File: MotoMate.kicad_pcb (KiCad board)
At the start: 2 copper layers, 92.3 x 50.2 mm, 62 parts, among them CN1 Cin1, CN2 Cin2, J1 Prog, J2 uUSB, J3 microSD, J4 GPS, J5 AUX_UART, J6 AUX_I2C, J7 Battery, J8 ILI9341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

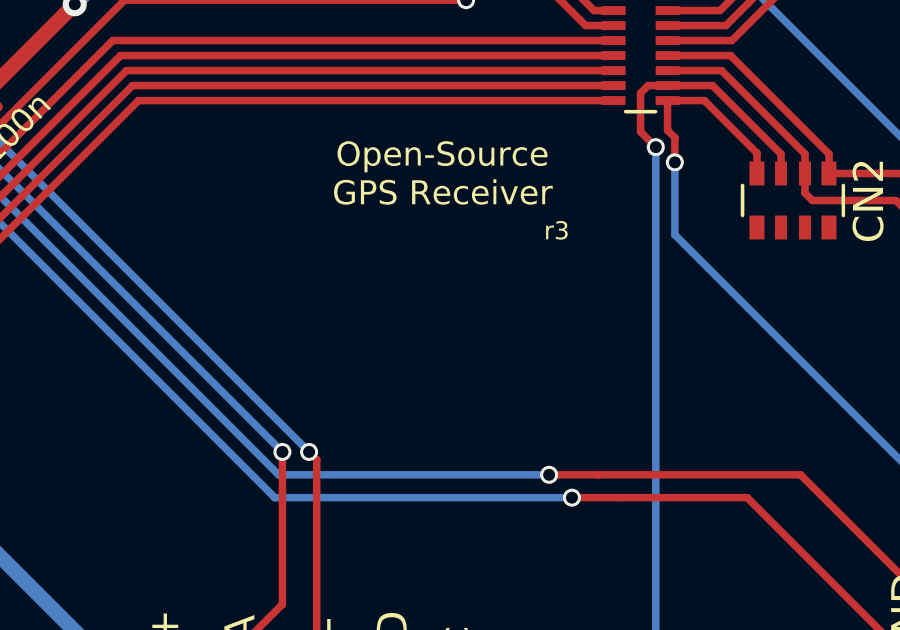
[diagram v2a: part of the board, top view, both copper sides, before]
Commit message: Re-add the OSHW logo
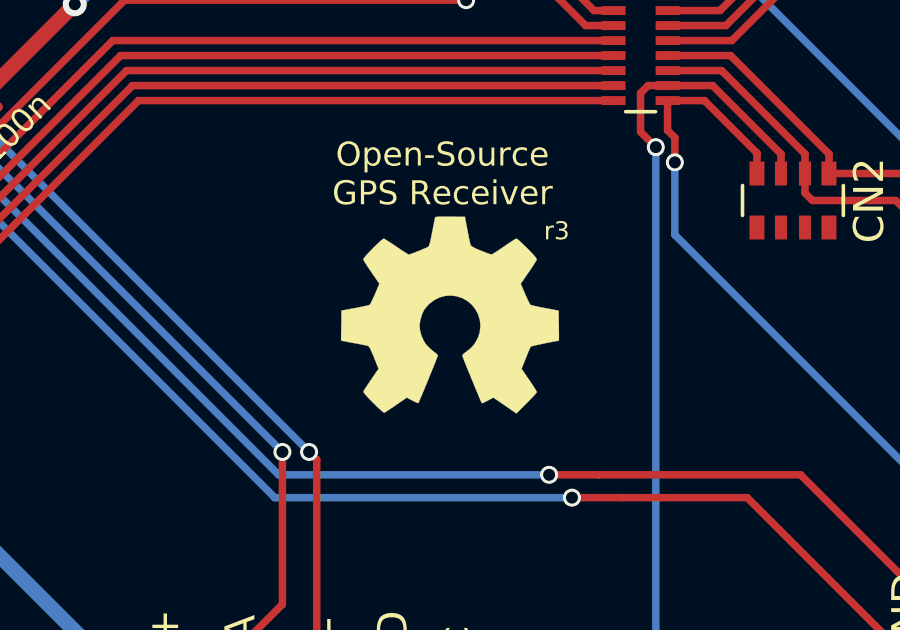
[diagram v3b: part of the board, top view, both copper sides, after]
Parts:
- added G***: LOGO, MotoMate:oshw_logo, F.Cu at (186.7, 77.5)
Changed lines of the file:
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@@
     (tracks 917)
     (zones 0)
-    (modules 62)
+    (modules 63)
     (nets 83)
   )
@@
     (add_net VPP)
   )
+  (module MotoMate:oshw_logo (layer F.Cu)
+    (at 186.69 77.47)
+    (fp_text reference G*** (at 0 0) (layer F.SilkS) hide
+      (effects (font (size 1.524 1.524) (thickness 0.3)))
+    )
+    (fp_text value LOGO (at 0.75 0) (layer F.SilkS) hide
+      (effects (font (size 1.524 1.524) (thickness 0.3)))
+    )
+    (fp_poly (pts (xy -0.001939 -3.270909) (xy 0.005764 -3.270801) (xy 0.4953 -3.2639) (xy 0.579721 -2.8194)
+      (xy 0.608349 -2.671878) (xy 0.635306 -2.538837) (xy 0.65863 -2.429529) (xy 0.676356 -2.353204)
+      (xy 0.685449 -2.321432) (xy 0.713175 -2.289694) (xy 0.776545 -2.249776) (xy 0.879824 -2.199374)
+      (xy 1.027272 -2.136179) (xy 1.029728 -2.135169) (xy 1.15085 -2.087336) (xy 1.257547 -2.04886)
+      (xy 1.339942 -2.023038) (xy 1.388153 -2.013166) (xy 1.393899 -2.013627) (xy 1.427416 -2.031241)
+      (xy 1.494903 -2.073143) (xy 1.58878 -2.1344) (xy 1.701463 -2.210075) (xy 1.80693 -2.28244)
+      (xy 1.928997 -2.365689) (xy 2.038229 -2.437731) (xy 2.127224 -2.493879) (xy 2.188579 -2.529446)
+      (xy 2.213696 -2.54) (xy 2.242052 -2.522762) (xy 2.299516 -2.474874) (xy 2.379752 -2.402074)
+      (xy 2.47642 -2.310101) (xy 2.575706 -2.2122) (xy 2.701787 -2.083829) (xy 2.793194 -1.985805)
+      (xy 2.852997 -1.91447) (xy 2.884263 -1.866168) (xy 2.890147 -1.83755) (xy 2.872121 -1.802199)
+      (xy 2.829861 -1.732905) (xy 2.768286 -1.637324) (xy 2.692319 -1.523113) (xy 2.617099 -1.412738)
+      (xy 2.356683 -1.034776) (xy 2.501389 -0.696433) (xy 2.555022 -0.574004) (xy 2.603918 -0.467843)
+      (xy 2.643717 -0.387027) (xy 2.670055 -0.340633) (xy 2.675597 -0.333941) (xy 2.709057 -0.321745)
+      (xy 2.784016 -0.302591) (xy 2.891956 -0.278395) (xy 3.024359 -0.251073) (xy 3.1623 -0.224478)
+      (xy 3.6195 -0.139163) (xy 3.626386 0.362218) (xy 3.628161 0.51557) (xy 3.629083 0.650005)
+      (xy 3.629152 0.757865) (xy 3.628369 0.831491) (xy 3.626732 0.863226) (xy 3.626386 0.863905)
+      (xy 3.582536 0.869733) (xy 3.50201 0.883911) (xy 3.394426 0.90444) (xy 3.269404 0.929321)
+      (xy 3.136562 0.956556) (xy 3.00552 0.984146) (xy 2.885896 1.010093) (xy 2.78731 1.032399)
+      (xy 2.719379 1.049066) (xy 2.691731 1.058086) (xy 2.675544 1.088124) (xy 2.644623 1.156695)
+      (xy 2.602744 1.255029) (xy 2.553685 1.374352) (xy 2.527477 1.43956) (xy 2.383858 1.799621)
+      (xy 2.639729 2.173967) (xy 2.722226 2.296162) (xy 2.793661 2.404835) (xy 2.849413 2.492721)
+      (xy 2.884864 2.552559) (xy 2.8956 2.57626) (xy 2.878389 2.602167) (xy 2.830485 2.657589)
+      (xy 2.757481 2.736488) (xy 2.66497 2.832826) (xy 2.558543 2.940564) (xy 2.55338 2.94572)
+      (xy 2.21116 3.287236) (xy 2.06443 3.186023) (xy 1.979463 3.127528) (xy 1.869485 3.051972)
+      (xy 1.751414 2.970975) (xy 1.681225 2.922885) (xy 1.444751 2.76096) (xy 1.257688 2.859826)
+      (xy 1.170833 2.903627) (xy 1.102259 2.934266) (xy 1.063141 2.946896) (xy 1.058505 2.946196)
+      (xy 1.044731 2.918832) (xy 1.014818 2.851109) (xy 0.971539 2.749797) (xy 0.917669 2.621662)
+      (xy 0.855979 2.473475) (xy 0.789244 2.312004) (xy 0.720237 2.144016) (xy 0.651732 1.976281)
+      (xy 0.5865 1.815567) (xy 0.527316 1.668643) (xy 0.476954 1.542276) (xy 0.438186 1.443237)
+      (xy 0.413785 1.378293) (xy 0.406399 1.354673) (xy 0.42587 1.326194) (xy 0.477269 1.279263)
+      (xy 0.550078 1.223339) (xy 0.561286 1.215397) (xy 0.657603 1.137446) (xy 0.752579 1.043801)
+      (xy 0.815737 0.96771) (xy 0.926687 0.774169) (xy 0.991201 0.574611) (xy 1.012403 0.374192)
+      (xy 0.993413 0.178067) (xy 0.937354 -0.008608) (xy 0.847346 -0.180679) (xy 0.726512 -0.33299)
+      (xy 0.577973 -0.460386) (xy 0.404851 -0.557712) (xy 0.210268 -0.619813) (xy -0.002655 -0.641533)
+      (xy -0.152432 -0.631146) (xy -0.34424 -0.581057) (xy -0.529533 -0.488363) (xy -0.69661 -0.360995)
+      (xy -0.833772 -0.206882) (xy -0.877537 -0.1397) (xy -0.935421 -0.013631) (xy -0.981769 0.138774)
+      (xy -1.010181 0.293308) (xy -1.016 0.384073) (xy -0.998901 0.534281) (xy -0.952151 0.699391)
+      (xy -0.882577 0.858946) (xy -0.826104 0.953262) (xy -0.758022 1.036062) (xy -0.666673 1.126589)
+      (xy -0.571704 1.205391) (xy -0.570725 1.206111) (xy -0.493874 1.265954) (xy -0.436246 1.317344)
+      (xy -0.407792 1.351202) (xy -0.406401 1.356028) (xy -0.415739 1.384849) (xy -0.441905 1.453772)
+      (xy -0.482125 1.55603) (xy -0.533625 1.684861) (xy -0.593631 1.833497) (xy -0.659369 1.995175)
+      (xy -0.728066 2.16313) (xy -0.796947 2.330597) (xy -0.863239 2.490811) (xy -0.924167 2.637006)
+      (xy -0.976958 2.762419) (xy -1.018838 2.860285) (xy -1.047034 2.923838) (xy -1.058383 2.946073)
+      (xy -1.084636 2.940636) (xy -1.144059 2.915353) (xy -1.225471 2.875146) (xy -1.255512 2.859305)
+      (xy -1.440643 2.760163) (xy -1.799577 3.006385) (xy -1.919676 3.088227) (xy -2.026539 3.160026)
+      (xy -2.112593 3.216776) (xy -2.170267 3.253471) (xy -2.190558 3.264904) (xy -2.217706 3.251586)
+      (xy -2.274116 3.20717) (xy -2.353693 3.137038) (xy -2.450343 3.046568) (xy -2.55797 2.941141)
+      (xy -2.562731 2.936374) (xy -2.68938 2.807743) (xy -2.781862 2.709493) (xy -2.843477 2.637701)
+      (xy -2.877527 2.588442) (xy -2.88731 2.557793) (xy -2.886099 2.551876) (xy -2.866615 2.517068)
+      (xy -2.823339 2.44848) (xy -2.761456 2.354055) (xy -2.686152 2.241737) (xy -2.626638 2.154401)
+      (xy -2.383935 1.800596) (xy -2.531299 1.430496) (xy -2.597902 1.26882) (xy -2.651199 1.152357)
+      (xy -2.692877 1.077785) (xy -2.724621 1.041779) (xy -2.729982 1.03889) (xy -2.774354 1.026225)
+      (xy -2.856941 1.00775) (xy -2.965843 0.98597) (xy -3.0861 0.963926) (xy -3.218262 0.940377)
+      (xy -3.344633 0.91721) (xy -3.449792 0.897289) (xy -3.51208 0.884816) (xy -3.633259 0.859163)
+      (xy -3.62638 0.36) (xy -3.6195 -0.139163) (xy -3.1623 -0.224478) (xy -3.014768 -0.252988)
+      (xy -2.883757 -0.280158) (xy -2.777787 -0.304072) (xy -2.705376 -0.322815) (xy -2.675598 -0.333941)
+      (xy -2.65547 -0.364992) (xy -2.620237 -0.433889) (xy -2.57426 -0.531554) (xy -2.521902 -0.648912)
+      (xy -2.50139 -0.696433) (xy -2.356684 -1.034776) (xy -2.6171 -1.412738) (xy -2.701694 -1.537044)
+      (xy -2.776247 -1.64949) (xy -2.835837 -1.742419) (xy -2.875543 -1.808175) (xy -2.890148 -1.83755)
+      (xy -2.883993 -1.866736) (xy -2.852324 -1.915353) (xy -2.792074 -1.987059) (xy -2.700173 -2.085508)
+      (xy -2.575707 -2.2122) (xy -2.469506 -2.316853) (xy -2.37393 -2.407687) (xy -2.295293 -2.478967)
+      (xy -2.239912 -2.524955) (xy -2.214783 -2.540001) (xy -2.183934 -2.526221) (xy -2.118643 -2.48791)
+      (xy -2.026126 -2.429613) (xy -1.913597 -2.355873) (xy -1.79129 -2.273301) (xy -1.666651 -2.188962)
+      (xy -1.55551 -2.115596) (xy -1.464949 -2.057729) (xy -1.402052 -2.01989) (xy -1.374053 -2.006601)
+      (xy -1.337635 -2.01602) (xy -1.265961 -2.041229) (xy -1.170316 -2.07765) (xy -1.061982 -2.120709)
+      (xy -0.952243 -2.165829) (xy -0.852384 -2.208435) (xy -0.773689 -2.243952) (xy -0.72744 -2.267802)
+      (xy -0.723634 -2.270354) (xy -0.703291 -2.299447) (xy -0.680936 -2.360954) (xy -0.655335 -2.459537)
+      (xy -0.625252 -2.59986) (xy -0.595395 -2.75458) (xy -0.567555 -2.901745) (xy -0.542043 -3.032893)
+      (xy -0.520609 -3.139317) (xy -0.505002 -3.212311) (xy -0.497387 -3.242223) (xy -0.484192 -3.254736)
+      (xy -0.451527 -3.263685) (xy -0.39318 -3.269425) (xy -0.302941 -3.272307) (xy -0.174598 -3.272684)
+      (xy -0.001939 -3.270909)) (layer F.SilkS) (width 0.01))
+  )
   (module MotoMate:LQFP-64_10x10mm_P0.5mm (layer F.Cu)
